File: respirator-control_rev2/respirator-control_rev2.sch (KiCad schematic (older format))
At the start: 36 parts, among them J1 Conn_01x02, J2 Header 1X4, J3 Header 1X3, J4 Header 1X3, J5 Header 1X4, J6 Header 1X30, SW1 SW_Push_Dual, SW2 SW_Push, SW3 SW_Push_Dual, U1 LCD-016N002L

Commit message: Add files via upload
Change Connectors to horizontal from veritical add Point To secure Cables .
add JPG to Sch to show How to secure Cables.

Gerber in Not Updated  and Not Checked In Fusion  .
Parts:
- removed H4: MountingHole, MountingHole:MountingHole_3.2mm_M3, symbol Mechanical:MountingHole
- J3, J4: footprint Connector_PinHeader_2.54mm:PinHeader_1x03_P2.54mm_Vertical -> Connector_PinHeader_2.54mm:PinHeader_1x03_P2.54mm_Horizontal
- J5: footprint Connector_PinHeader_2.54mm:PinHeader_1x04_P2.54mm_Vertical -> Connector_PinHeader_2.54mm:PinHeader_1x04_P2.54mm_Horizontal
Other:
- note added: "J2 needs To Be Hot Glued or Silcon both ends also on the LCD Side"
- note added: "Secure The wires as Shown do not damage the wires"
- note added: "USB can be added if permanent connected"
- note added: "it is to relieve Strain"

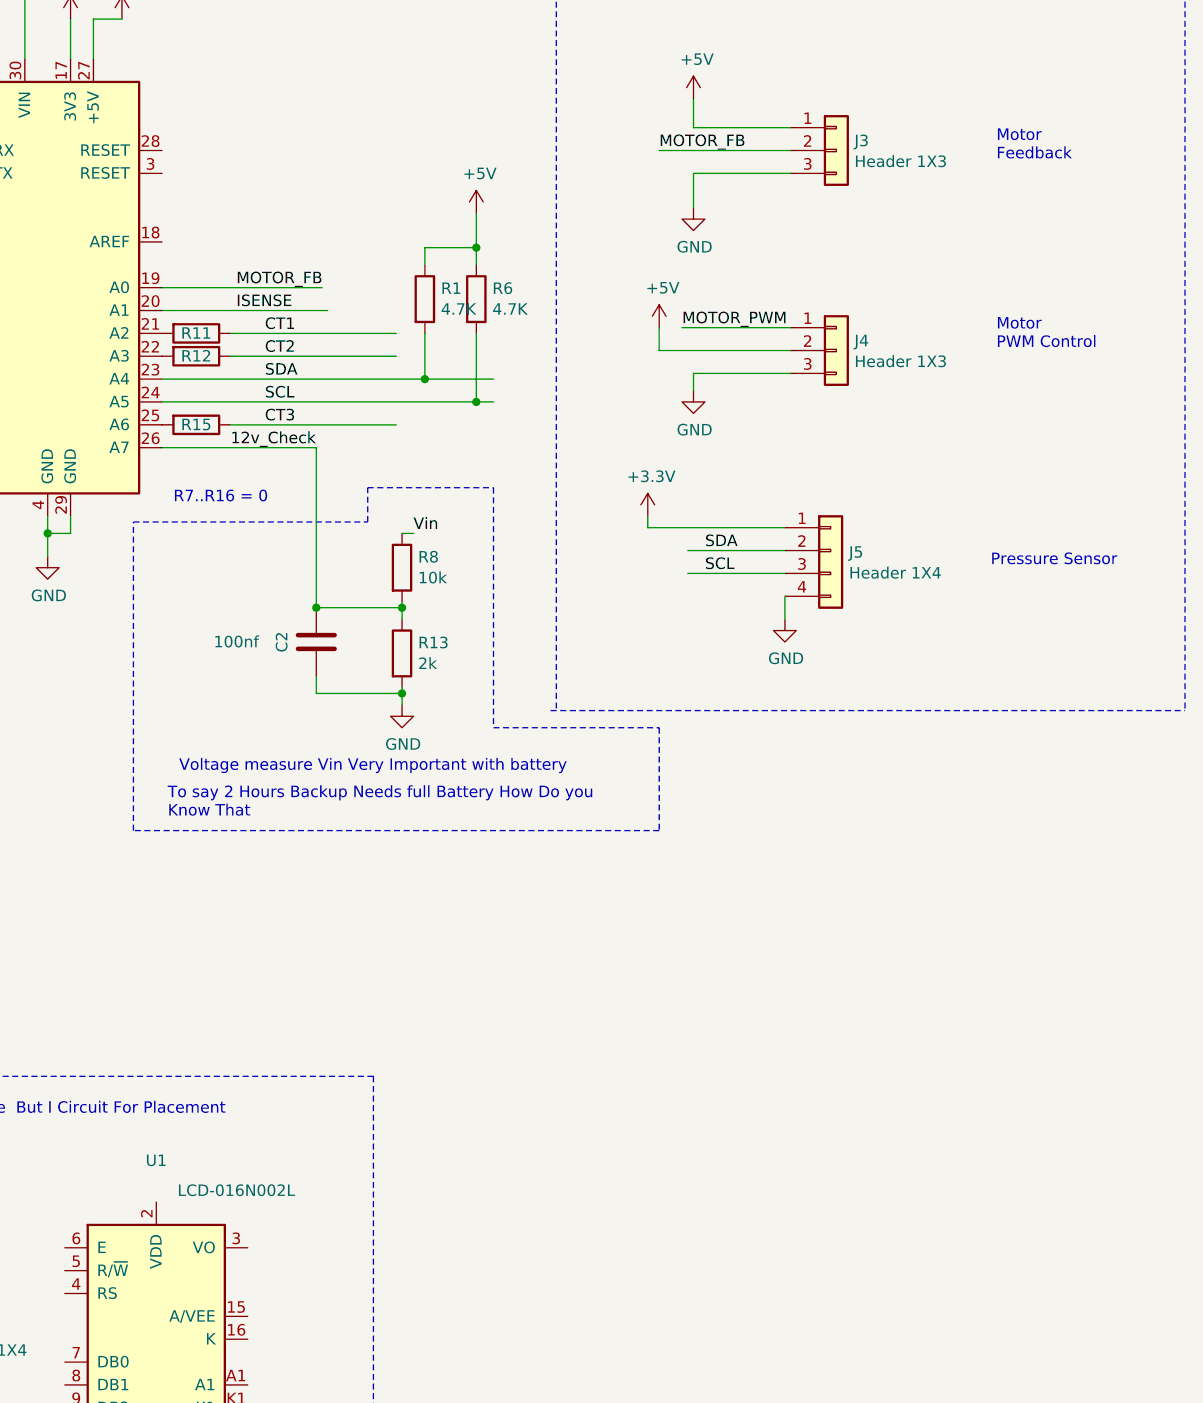
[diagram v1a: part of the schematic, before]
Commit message: Add files via upload
Add level convert SCL SDA
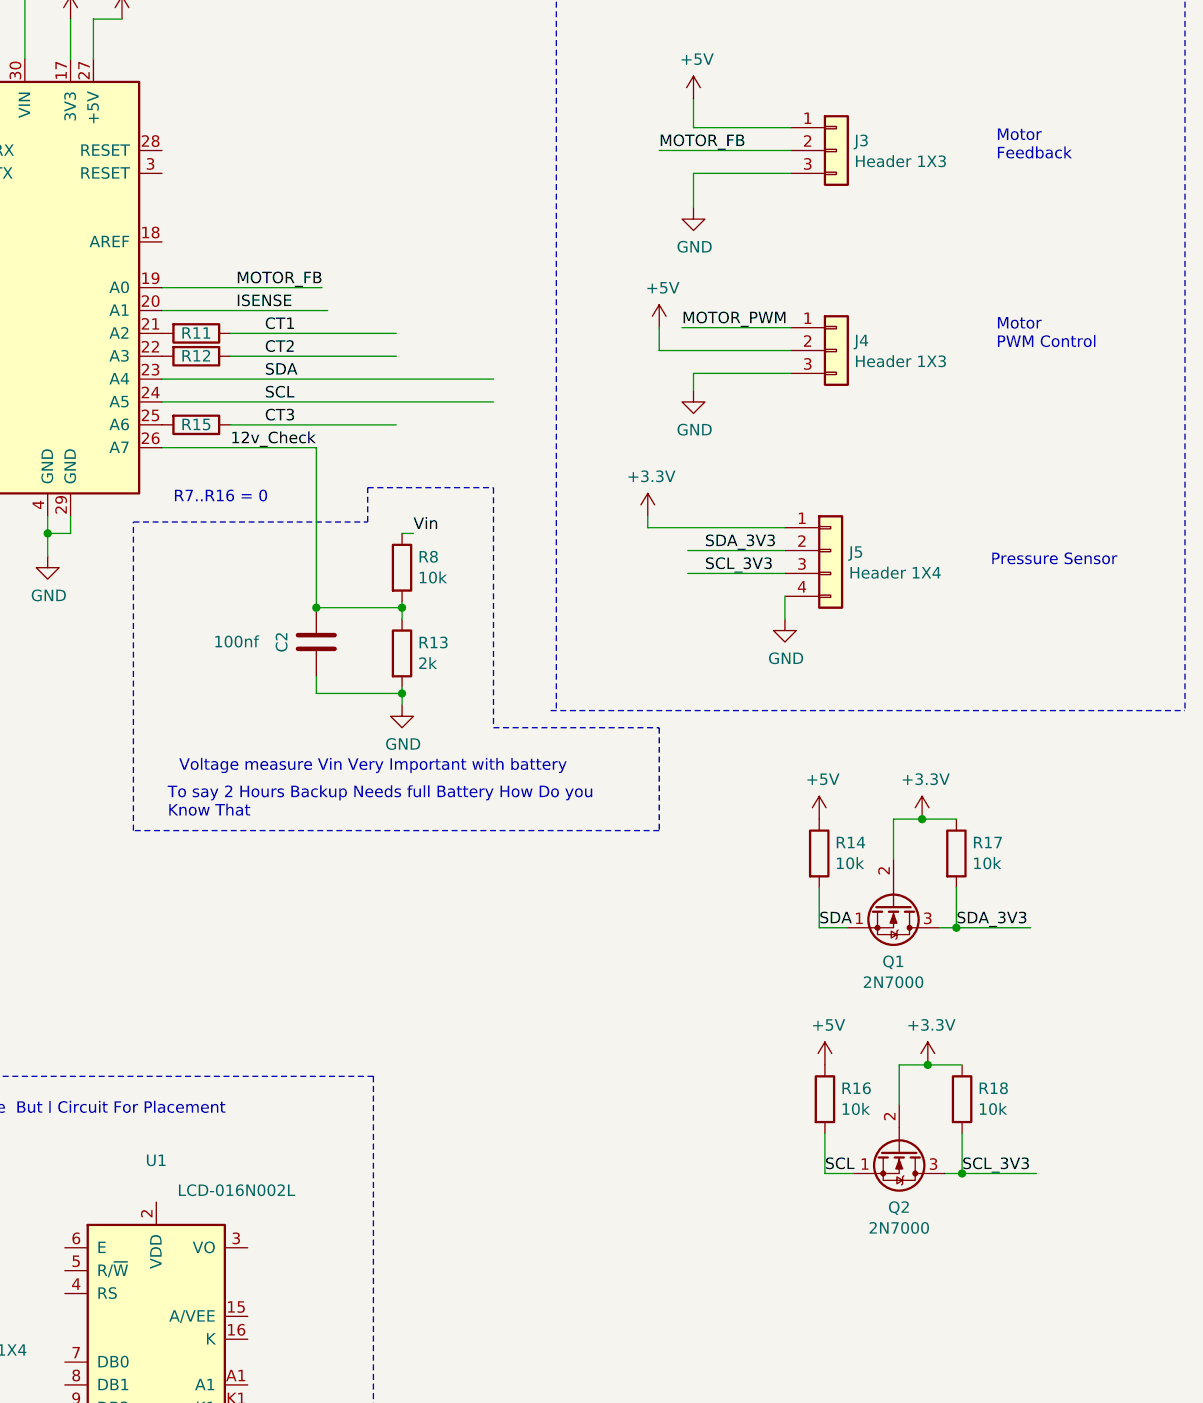
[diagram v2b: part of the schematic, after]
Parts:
- removed R1, R6: 4.7K, Resistor_THT:R_Axial_DIN0207_L6.3mm_D2.5mm_P7.62mm_Horizontal, symbol Device:R
- added Q1, Q2: 2N7000, Package_TO_SOT_THT:TO-92_Inline, symbol Transistor_FET:2N7000
- added R14, R16, R17, R18: 10k, Resistor_THT:R_Axial_DIN0207_L6.3mm_D2.5mm_P7.62mm_Horizontal, symbol Device:R
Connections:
- net labels added: SCL_3V3, SDA_3V3
- wire segments 163 -> 171
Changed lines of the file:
@@
 	13475 4300 13050 4300
 Text Label 13125 4300 0    50   ~ 0
-SDA
+SDA_3V3
 Text Label 13125 4400 0    50   ~ 0
-SCL
-Wire Wire Line
-	11900 3550 11900 3350
-Wire Wire Line
-	12125 3650 12125 3350
-$Comp
-L Device:R R1
-U 1 1 5E91ED0A
-P 11900 3200
-F 0 "R1" H 11970 3246 50  0000 L CNN
-F 1 "4.7K" H 11970 3155 50  0000 L CNN
-F 2 "Resistor_THT:R_Axial_DIN0207_L6.3mm_D2.5mm_P7.62mm_Horizontal" V 11830 3200 50  0001 C CNN
-F 3 "~" H 11900 3200 50  0001 C CNN
-	1    11900 3200
-	1    0    0    -1
-$EndComp
-$Comp
-L Device:R R6
-U 1 1 5E91ED66
-P 12125 3200
-F 0 "R6" H 12195 3246 50  0000 L CNN
-F 1 "4.7K" H 12195 3155 50  0000 L CNN
-F 2 "Resistor_THT:R_Axial_DIN0207_L6.3mm_D2.5mm_P7.62mm_Horizontal" V 12055 3200 50  0001 C CNN
-F 3 "~" H 12125 3200 50  0001 C CNN
-	1    12125 3200
-	1    0    0    -1
-$EndComp
-Wire Wire Line
-	11900 3050 11900 2975
-Wire Wire Line
-	11900 2975 12125 2975
-Wire Wire Line
-	12125 2975 12125 3050
-Wire Wire Line
-	12125 2975 12125 2825
-Connection ~ 12125 2975
-$Comp
-L power:+5V #PWR0110
-U 1 1 5E92DC49
-P 12125 2825
-F 0 "#PWR0110" H 12125 2675 50  0001 C CNN
-F 1 "+5V" H 12140 2998 50  0000 C CNN
-F 2 "" H 12125 2825 50  0001 C CNN
-F 3 "" H 12125 2825 50  0001 C CNN
-	1    12125 2825
-	1    0    0    -1
-$EndComp
+SCL_3V3
 $Comp
 L Device:R R7
@@
 	6900 3225 6900 4125
 Wire Wire Line
-	10750 3550 11900 3550
-Wire Wire Line
-	10750 3650 12125 3650
-Wire Wire Line
-	12200 3550 11900 3550
-Connection ~ 11900 3550
-Wire Wire Line
-	12200 3650 12125 3650
-Connection ~ 12125 3650
-Wire Wire Line
 	12875 4200 13475 4200
 Wire Wire Line
@@
 Text Notes 12550 1400 0    50   ~ 0
 USB can be added if permanent connected
+$Comp
+L Transistor_FET:2N7000 Q1
+U 1 1 5EAFB051
+P 13950 5850
+F 0 "Q1" V 14199 5850 50  0000 C CNN
+F 1 "2N7000" V 14290 5850 50  0000 C CNN
+F 2 "Package_TO_SOT_THT:TO-92_Inline" H 14150 5775 50  0001 L CIN
+F 3 "https://www.fairchildsemi.com/datasheets/2N/2N7000.pdf" H 13950 5850 50  0001 L CNN
+	1    13950 5850
+	0    1    1    0
+$EndComp
+$Comp
+L Device:R R14
+U 1 1 5EAFDB3D
+P 13625 5625
+F 0 "R14" H 13695 5671 50  0000 L CNN
+F 1 "10k" H 13695 5580 50  0000 L CNN
+F 2 "Resistor_THT:R_Axial_DIN0207_L6.3mm_D2.5mm_P7.62mm_Horizontal" V 13555 5625 50  0001 C CNN
+F 3 "~" H 13625 5625 50  0001 C CNN
+	1    13625 5625
+	1    0    0    -1
+$EndComp
+$Comp
+L Device:R R17
+U 1 1 5EAFEDE1
+P 14225 5625
+F 0 "R17" H 14295 5671 50  0000 L CNN
+F 1 "10k" H 14295 5580 50  0000 L CNN
+F 2 "Resistor_THT:R_Axial_DIN0207_L6.3mm_D2.5mm_P7.62mm_Horizontal" V 14155 5625 50  0001 C CNN
+F 3 "~" H 14225 5625 50  0001 C CNN
+	1    14225 5625
+	1    0    0    -1
+$EndComp
+Wire Wire Line
+	13625 5775 13625 5950
+Wire Wire Line
+	13625 5950 13750 5950
+Wire Wire Line
+	14150 5950 14225 5950
+Wire Wire Line
+	14225 5950 14225 5775
+Wire Wire Line
+	13950 5650 13950 5475
+Wire Wire Line
+	13950 5475 14075 5475
+$Comp
+L power:+3.3V #PWR0102
+U 1 1 5EB1C49A
+P 14075 5475
+F 0 "#PWR0102" H 14075 5325 50  0001 C CNN
+F 1 "+3.3V" H 14090 5648 50  0000 C CNN
+F 2 "" H 14075 5475 50  0001 C CNN
+F 3 "" H 14075 5475 50  0001 C CNN
+	1    14075 5475
+	1    0    0    -1
+$EndComp
+Connection ~ 14075 5475
+Wire Wire Line
+	14075 5475 14225 5475
+$Comp
+L power:+5V #PWR0114
+U 1 1 5EB1D9D3
+P 13625 5475
+F 0 "#PWR0114" H 13625 5325 50  0001 C CNN
+F 1 "+5V" H 13640 5648 50  0000 C CNN
+F 2 "" H 13625 5475 50  0001 C CNN
+F 3 "" H 13625 5475 50  0001 C CNN
+	1    13625 5475
+	1    0    0    -1
+$EndComp
+$Comp
+L Transistor_FET:2N7000 Q2
+U 1 1 5EB209A7
+P 13975 6925
+F 0 "Q2" V 14224 6925 50  0000 C CNN
+F 1 "2N7000" V 14315 6925 50  0000 C CNN
+F 2 "Package_TO_SOT_THT:TO-92_Inline" H 14175 6850 50  0001 L CIN
+F 3 "https://www.fairchildsemi.com/datasheets/2N/2N7000.pdf" H 13975 6925 50  0001 L CNN
+	1    13975 6925
+	0    1    1    0
+$EndComp
+$Comp
+L Device:R R16
+U 1 1 5EB209AD
+P 13650 6700
+F 0 "R16" H 13720 6746 50  0000 L CNN
+F 1 "10k" H 13720 6655 50  0000 L CNN
+F 2 "Resistor_THT:R_Axial_DIN0207_L6.3mm_D2.5mm_P7.62mm_Horizontal" V 13580 6700 50  0001 C CNN
+F 3 "~" H 13650 6700 50  0001 C CNN
+	1    13650 6700
+	1    0    0    -1
+$EndComp
+$Comp
+L Device:R R18
+U 1 1 5EB209B3
+P 14250 6700
+F 0 "R18" H 14320 6746 50  0000 L CNN
+F 1 "10k" H 14320 6655 50  0000 L CNN
+F 2 "Resistor_THT:R_Axial_DIN0207_L6.3mm_D2.5mm_P7.62mm_Horizontal" V 14180 6700 50  0001 C CNN
+F 3 "~" H 14250 6700 50  0001 C CNN
+	1    14250 6700
+	1    0    0    -1
+$EndComp
+Wire Wire Line
+	13650 6850 13650 7025
+Wire Wire Line
+	13650 7025 13775 7025
+Wire Wire Line
+	14175 7025 14250 7025
+Wire Wire Line
+	14250 7025 14250 6850
+Wire Wire Line
+	13975 6725 13975 6550
+Wire Wire Line
+	13975 6550 14100 6550
+$Comp
+L power:+3.3V #PWR0116
+U 1 1 5EB209BF
+P 14100 6550
+F 0 "#PWR0116" H 14100 6400 50  0001 C CNN
+F 1 "+3.3V" H 14115 6723 50  0000 C CNN
+F 2 "" H 14100 6550 50  0001 C CNN
+F 3 "" H 14100 6550 50  0001 C CNN
+	1    14100 6550
+	1    0    0    -1
+$EndComp
+Connection ~ 14100 6550
+Wire Wire Line
+	14100 6550 14250 6550
+$Comp
+L power:+5V #PWR0118
+U 1 1 5EB209C7
+P 13650 6550
+F 0 "#PWR0118" H 13650 6400 50  0001 C CNN
+F 1 "+5V" H 13665 6723 50  0000 C CNN
+F 2 "" H 13650 6550 50  0001 C CNN
+F 3 "" H 13650 6550 50  0001 C CNN
+	1    13650 6550
+	1    0    0    -1
+$EndComp
+Text Label 14250 7025 0    50   ~ 0
+SCL_3V3
+Text Label 13650 7025 0    50   ~ 0
+SCL
+Text Label 14225 5950 0    50   ~ 0
+SDA_3V3
+Text Label 13625 5950 0    50   ~ 0
+SDA
+Wire Wire Line
+	10750 3650 12200 3650
+Wire Wire Line
+	10750 3550 12200 3550
+Wire Wire Line
+	14225 5950 14550 5950
+Connection ~ 14225 5950
+Wire Wire Line
+	14250 7025 14575 7025
+Connection ~ 14250 7025
 $EndSCHEMATC
